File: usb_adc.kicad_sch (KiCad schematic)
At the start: 23 parts, among them IC1 PCM2903CDBR, SW1 SW_Push, SW2 SW_Push, SW3 SW_Push, U1 74LVC1G08, X1 ECS-120-8-36-CKM-TR3

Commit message: Resnap text to grid + add .gitignore
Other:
- company: (none) -> Tachyon PCBAs
- title: (none) -> USB ADC
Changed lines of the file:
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@@
 	(paper "A4")
 	(title_block
-		(date "2024-09-12")
+		(title "USB ADC")
+		(date "2024-09-15")
+		(rev "1")
+		(company "Tachyon PCBAs")
+		(comment 1 "first try surely")
+		(comment 2 "Built around the PCM2903C")
 	)
 	(junction
@@
 	(text "USB ADC"
 		(exclude_from_sim no)
-		(at 111.76 49.022 0)
+		(at 111.76 48.895 0)
 		(effects
 			(font
@@
 	(text "Pierce Oscillator (12MHz)"
 		(exclude_from_sim no)
-		(at 178.054 113.538 0)
+		(at 177.8 113.665 0)
 		(effects
 			(font
@@
 	(text "USB D+ Pull Up Logic"
 		(exclude_from_sim no)
-		(at 177.8 61.468 0)
+		(at 177.8 61.595 0)
 		(effects
 			(font
@@
 	(text "Suspension Indication LED"
 		(exclude_from_sim no)
-		(at 142.748 69.85 90)
+		(at 142.875 69.85 90)
 		(effects
 			(font
@@
 	(text "State machine control (Mute, Volume adj.)"
 		(exclude_from_sim no)
-		(at 178.054 17.018 0)
+		(at 177.8 17.145 0)
 		(effects
 			(font

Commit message: Started defining components
Man going down the capacitor dielectric rabbit hole eats up SO MUCH TIME
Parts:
- C1, C3, C4, C5: footprint Capacitor_SMD:C_0603_1608Metric_Pad1.08x0.95mm_HandSolder -> Capacitor_SMD:C_0805_2012Metric_Pad1.18x1.45mm_HandSolder; Mouser Part Number (none) -> 581-TAJA106K010TNJ
- C2: footprint (none) -> Capacitor_SMD:C_0805_2012Metric_Pad1.18x1.45mm_HandSolder; Mouser Part Number (none) -> 74-TMCP1E104KTRF
- C6, C7: Mouser Part Number (none) -> 581-06035A160FAT2A
- D1: value LED -> LTST-C193KRKT-2A; Mouser Part Number (none) -> 859-LTST-C193KRKT-2A
- R1, R10, R2, R4, R5, R6, R7, R8: footprint (none) -> Resistor_SMD:R_0603_1608Metric_Pad0.98x0.95mm_HandSolder
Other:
- moved on the sheet: D1
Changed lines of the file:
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@@
 	(wire
 		(pts
-			(xy 130.81 71.12) (xy 132.08 71.12)
+			(xy 133.35 71.12) (xy 132.08 71.12)
 		)
 		(stroke
@@
 	)
 	(label "~{SSPND}_R"
-		(at 130.81 71.12 180)
+		(at 133.35 71.12 0)
 		(fields_autoplaced yes)
 		(effects
@@
 				(size 1.27 1.27)
 			)
-			(justify right bottom)
+			(justify left bottom)
 		)
 	)
@@
 			)
 		)
-		(property "Footprint" "Capacitor_SMD:C_0603_1608Metric_Pad1.08x0.95mm_HandSolder"
+		(property "Footprint" "Capacitor_SMD:C_0805_2012Metric_Pad1.18x1.45mm_HandSolder"
 			(at 144.4752 119.38 0)
 			(effects
@@
 			)
 		)
-		(property "Datasheet" "~"
+		(property "Datasheet" "https://www.mouser.com/datasheet/2/40/TAJ_AUTO-3165268.pdf"
 			(at 143.51 115.57 0)
 			(effects
@@
 			)
 		)
+		(property "Mouser Part Number" "581-TAJA106K010TNJ"
+			(at 143.51 115.57 0)
+			(effects
+				(font
+					(size 1.27 1.27)
+				)
+				(hide yes)
+			)
+		)
 		(pin "1"
 		)
@@
 			)
 		)
-		(property "Footprint" "Capacitor_SMD:C_0603_1608Metric_Pad1.08x0.95mm_HandSolder"
+		(property "Footprint" "Capacitor_SMD:C_0805_2012Metric_Pad1.18x1.45mm_HandSolder"
 			(at 150.8252 93.98 0)
 			(effects
@@
 			)
 		)
-		(property "Datasheet" "~"
+		(property "Datasheet" "https://www.mouser.com/datasheet/2/40/TAJ_AUTO-3165268.pdf"
 			(at 149.86 90.17 0)
 			(effects
@@
 			)
 		)
+		(property "Mouser Part Number" "581-TAJA106K010TNJ"
+			(at 149.86 90.17 0)
+			(effects
+				(font
+					(size 1.27 1.27)
+				)
+				(hide yes)
+			)
+		)
 		(pin "1"
 		)
@@
 			)
 		)
-		(property "Footprint" ""
+		(property "Footprint" "Resistor_SMD:R_0603_1608Metric_Pad0.98x0.95mm_HandSolder"
 			(at 207.772 33.02 90)
 			(effects
@@
 			)
 		)
-		(property "Datasheet" "~"
+		(property "Datasheet" "https://www.mouser.com/datasheet/2/40/C0GNP0_Dielectric-2952720.pdf"
 			(at 223.52 147.32 0)
 			(effects
@@
 			)
 		)
+		(property "Mouser Part Number" "581-06035A160FAT2A"
+			(at 223.52 147.32 0)
+			(effects
+				(font
+					(size 1.27 1.27)
+				)
+				(hide yes)
+			)
+		)
 		(pin "1"
 		)
@@
 			)
 		)
-		(property "Footprint" ""
+		(property "Footprint" "Resistor_SMD:R_0603_1608Metric_Pad0.98x0.95mm_HandSolder"
 			(at 236.22 85.598 90)
 			(effects
@@
 			)
 		)
-		(property "Footprint" ""
+		(property "Footprint" "Capacitor_SMD:C_0805_2012Metric_Pad1.18x1.45mm_HandSolder"
 			(at 180.6448 73.66 0)
 			(effects
@@
 			)
 		)
-		(property "Datasheet" "~"
+		(property "Datasheet" "https://www.vishay.com/docs/40179/tmcp.pdf"
 			(at 181.61 77.47 0)
 			(effects
@@
 			)
 		)
+		(property "Mouser Part Number" "74-TMCP1E104KTRF"
+			(at 181.61 77.47 0)
+			(effects
+				(font
+					(size 1.27 1.27)
+				)
+				(hide yes)
+			)
+		)
 		(pin "2"
 		)
@@
 			)
 		)
-		(property "Footprint" ""
+		(property "Footprint" "Resistor_SMD:R_0603_1608Metric_Pad0.98x0.95mm_HandSolder"
 			(at 191.262 91.44 90)
 			(effects
@@
 	(symbol
 		(lib_id "Device:LED")
-		(at 132.08 66.04 90)
+		(at 132.08 66.04 270)
+		(mirror x)
 		(unit 1)
 		(exclude_from_sim no)
@@
 		(fields_autoplaced yes)
 		(property "Reference" "D1"
-			(at 135.89 66.3574 90)
+			(at 128.27 66.3574 90)
 			(effects
 				(font
@@
 			)
 		)
-		(property "Value" "LED"
-			(at 135.89 68.8974 90)
+		(property "Value" "LTST-C193KRKT-2A"
+			(at 128.27 68.8974 90)
 			(effects
 				(font
@@
 			)
 		)
-		(property "Datasheet" "~"
+		(property "Datasheet" "https://www.mouser.com/datasheet/2/239/lite-on_lite-s-a0004283979-1-1749859.pdf"
 			(at 132.08 66.04 0)
 			(effects
@@
 			)
 		)
+		(property "Mouser Part Number" "859-LTST-C193KRKT-2A"
+			(at 132.08 66.04 0)
+			(effects
+				(font
+					(size 1.27 1.27)
+				)
+				(hide yes)
+			)
+		)
 		(pin "2"
 		)
@@
 			)
 		)
-		(property "Footprint" ""
+		(property "Footprint" "Resistor_SMD:R_0603_1608Metric_Pad0.98x0.95mm_HandSolder"
 			(at 81.28 84.328 90)
 			(effects
@@
 			)
 		)
-		(property "Footprint" ""
+		(property "Footprint" "Resistor_SMD:R_0603_1608Metric_Pad0.98x0.95mm_HandSolder"
 			(at 182.372 33.02 90)
 			(effects
@@
 			)
 		)
-		(property "Footprint" "Capacitor_SMD:C_0603_1608Metric_Pad1.08x0.95mm_HandSolder"
+		(property "Footprint" "Capacitor_SMD:C_0805_2012Metric_Pad1.18x1.45mm_HandSolder"
 			(at 87.63 116.5352 0)
 			(effects
@@
 			)
 		)
-		(property "Datasheet" "~"
+		(property "Datasheet" "https://www.mouser.com/datasheet/2/40/TAJ_AUTO-3165268.pdf"
 			(at 83.82 115.57 0)
 			(effects
@@
 			)
 		)
+		(property "Mouser Part Number" "581-TAJA106K010TNJ"
+			(at 83.82 115.57 0)
+			(effects
+				(font
+					(size 1.27 1.27)
+				)
+				(hide yes)
+			)
+		)
 		(pin "1"
 		)
@@
 			)
 		)
-		(property "Footprint" ""
+		(property "Footprint" "Resistor_SMD:R_0603_1608Metric_Pad0.98x0.95mm_HandSolder"
 			(at 231.902 33.02 90)
 			(effects
@@
 		(lib_id "power:VDD")
 		(at 132.08 60.96 0)
+		(mirror y)
 		(unit 1)
 		(exclude_from_sim no)
@@
 			)
 		)
-		(property "Footprint" "Capacitor_SMD:C_0603_1608Metric_Pad1.08x0.95mm_HandSolder"
+		(property "Footprint" "Capacitor_SMD:C_0805_2012Metric_Pad1.18x1.45mm_HandSolder"
 			(at 64.4652 114.3 0)
 			(effects
@@
 			)
 		)
-		(property "Datasheet" "~"
+		(property "Datasheet" "https://www.mouser.com/datasheet/2/40/TAJ_AUTO-3165268.pdf"
 			(at 63.5 110.49 0)
 			(effects
@@
 			)
 		)
+		(property "Mouser Part Number" "581-TAJA106K010TNJ"
+			(at 63.5 110.49 0)
+			(effects
+				(font
+					(size 1.27 1.27)
+				)
+				(hide yes)
+			)
+		)
 		(pin "1"
 		)
@@
 			)
 		)
-		(property "Footprint" ""
+		(property "Footprint" "Resistor_SMD:R_0603_1608Metric_Pad0.98x0.95mm_HandSolder"
 			(at 81.28 86.868 90)
 			(effects
@@
 			)
 		)
-		(property "Datasheet" "~"
+		(property "Datasheet" "https://www.mouser.com/datasheet/2/40/C0GNP0_Dielectric-2952720.pdf"
 			(at 200.66 147.32 0)
 			(effects
@@
 			)
 		)
+		(property "Mouser Part Number" "581-06035A160FAT2A"
+			(at 200.66 147.32 0)
+			(effects
+				(font
+					(size 1.27 1.27)
+				)
+				(hide yes)
+			)
+		)
 		(pin "1"
 		)
@@
 			)
 		)
-		(property "Footprint" ""
+		(property "Footprint" "Resistor_SMD:R_0603_1608Metric_Pad0.98x0.95mm_HandSolder"
 			(at 130.302 76.2 90)
 			(effects

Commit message: Fully define components
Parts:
- R1, R2, R4, R8: Mouser Part Number (none) -> 667-ERA-3AEB152V
- R10, R13: Mouser Part Number (none) -> 652-CR0603FX-1004ELF
- R5: Mouser Part Number (none) -> 71-CRCW08055K60FKEAC
- R6, R7: Mouser Part Number (none) -> 652-CR0603FX-22R0ELF
- U1: Mouser Part Number (none) -> 771-74LVC1G08GV
- X1: Mouser Part Number (none) -> 520-120-8-36-CKM-TR3
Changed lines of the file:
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@@
+			)
+		)
+		(property "Mouser Part Number" "771-74LVC1G08GV"
+			(at 209.55 83.82 0)
+			(effects
+				(font
+					(size 1.27 1.27)
+				)
+				(hide yes)
 			)
 		)
@@
 			)
 		)
-		(property "Datasheet" "~"
+		(property "Datasheet" "https://www.mouser.com/datasheet/2/315/AOA0000C307-1149632.pdf"
 			(at 209.55 33.02 0)
 			(effects
@@
 			)
 		)
+		(property "Mouser Part Number" "667-ERA-3AEB152V"
+			(at 209.55 33.02 0)
+			(effects
+				(font
+					(size 1.27 1.27)
+				)
+				(hide yes)
+			)
+		)
 		(pin "2"
 		)
@@
 			)
 		)
-		(property "Datasheet" "~"
+		(property "Datasheet" "https://www.mouser.com/datasheet/2/54/cr-1858361.pdf"
 			(at 212.09 124.46 0)
 			(effects
@@
 			)
 		)
+		(property "Mouser Part Number" "652-CR0603FX-1004ELF"
+			(at 212.09 124.46 0)
+			(effects
+				(font
+					(size 1.27 1.27)
+				)
+				(hide yes)
+			)
+		)
 		(pin "1"
 		)
@@
 			)
 		)
-		(property "Datasheet" "~"
+		(property "Datasheet" "https://www.mouser.com/datasheet/2/315/AOA0000C307-1149632.pdf"
 			(at 236.22 83.82 0)
 			(effects
@@
 			)
 		)
+		(property "Mouser Part Number" "667-ERA-3AEB152V"
+			(at 236.22 83.82 0)
+			(effects
+				(font
+					(size 1.27 1.27)
+				)
+				(hide yes)
+			)
+		)
 		(pin "2"
 		)
@@
 			)
 		)
-		(property "Datasheet" "~"
+		(property "Datasheet" "https://www.mouser.com/datasheet/2/54/cr-1858361.pdf"
 			(at 193.04 91.44 0)
 			(effects
@@
 		)
 		(property "Description" "Resistor"
+			(at 193.04 91.44 0)
+			(effects
+				(font
+					(size 1.27 1.27)
+				)
+				(hide yes)
+			)
+		)
+		(property "Mouser Part Number" "652-CR0603FX-1004ELF"
 			(at 193.04 91.44 0)
 			(effects
@@
 			)
 		)
-		(property "Datasheet" "~"
+		(property "Datasheet" "https://www.mouser.com/datasheet/2/54/cr-1858361.pdf"
 			(at 81.28 82.55 0)
 			(effects
@@
 			)
 		)
+		(property "Mouser Part Number" "652-CR0603FX-22R0ELF"
+			(at 81.28 82.55 0)
+			(effects
+				(font
+					(size 1.27 1.27)
+				)
+				(hide yes)
+			)
+		)
 		(pin "2"
 		)
@@
 			)
 		)
-		(property "Datasheet" "~"
+		(property "Datasheet" "https://www.mouser.com/datasheet/2/315/AOA0000C307-1149632.pdf"
 			(at 184.15 33.02 0)
 			(effects
@@
 		)
 		(property "Description" "Resistor"
+			(at 184.15 33.02 0)
+			(effects
+				(font
+					(size 1.27 1.27)
+				)
+				(hide yes)
+			)
+		)
+		(property "Mouser Part Number" "667-ERA-3AEB152V"
 			(at 184.15 33.02 0)
 			(effects
@@
 			)
 		)
+		(property "Mouser Part Number" "520-120-8-36-CKM-TR3"
+			(at 212.09 142.24 0)
+			(effects
+				(font
+					(size 1.27 1.27)
+				)
+				(hide yes)
+			)
+		)
 		(pin "2"
 		)
@@
 			)
 		)
-		(property "Datasheet" "~"
+		(property "Datasheet" "https://www.mouser.com/datasheet/2/315/AOA0000C307-1149632.pdf"
 			(at 233.68 33.02 0)
 			(effects
@@
 		)
 		(property "Description" "Resistor"
+			(at 233.68 33.02 0)
+			(effects
+				(font
+					(size 1.27 1.27)
+				)
+				(hide yes)
+			)
+		)
+		(property "Mouser Part Number" "667-ERA-3AEB152V"
 			(at 233.68 33.02 0)
 			(effects
@@
 			)
 		)
-		(property "Datasheet" "~"
+		(property "Datasheet" "https://www.mouser.com/datasheet/2/54/cr-1858361.pdf"
 			(at 81.28 85.09 0)
 			(effects
@@
 		)
 		(property "Description" "Resistor"
+			(at 81.28 85.09 0)
+			(effects
+				(font
+					(size 1.27 1.27)
+				)
+				(hide yes)
+			)
+		)
+		(property "Mouser Part Number" "652-CR0603FX-22R0ELF"
 			(at 81.28 85.09 0)
 			(effects
@@
 			)
 		)
-		(property "Datasheet" "~"
+		(property "Datasheet" "https://www.vishay.com/doc?28773"
 			(at 132.08 76.2 0)
 			(effects
@@
 			(at 132.08 76.2 0)
 			(effects
+				(font
+					(size 1.27 1.27)
+				)
+				(hide yes)
+			)
+		)
+		(property "Mouser Part Number" "71-CRCW08055K60FKEAC"
+			(at 132.08 76.2 0)
+			(effects

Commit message: Replace S/PIDF RCA jack with a singular one since I won't need an input one
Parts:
- SW1, SW2, SW3: value SW_Push -> MX1A-11NW; footprint (none) -> binauralmic:SW_MX; Mouser Part Number (none) -> 540-MX1A-11NW
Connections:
- net DIN: no longer names the net of IC1.24 (DIN)
- no-connect marks 2 -> 3
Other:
- moved on the sheet: R1, R2, R4, SW1, SW2, SW3

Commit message: Removing extraneous peripherals
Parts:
- removed R1, R2, R4: 1.5k, Resistor_SMD:R_0603_1608Metric_Pad0.98x0.95mm_HandSolder, symbol Device:R
- removed SW1, SW2, SW3: MX1A-11NW, binauralmic:SW_MX, symbol Switch:SW_Push
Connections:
- net HID0: no longer names the net of IC1.5 (HID0)
- net HID1: no longer names the net of IC1.6 (HID1)
- net HID2: no longer names the net of IC1.7 (HID2)
- no-connect marks 3 -> 6
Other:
- note removed: "State machine control (Mute, Volume adj.)"
- moved on the sheet: C2, C6, C7, R10, R13, R8, U1, X1

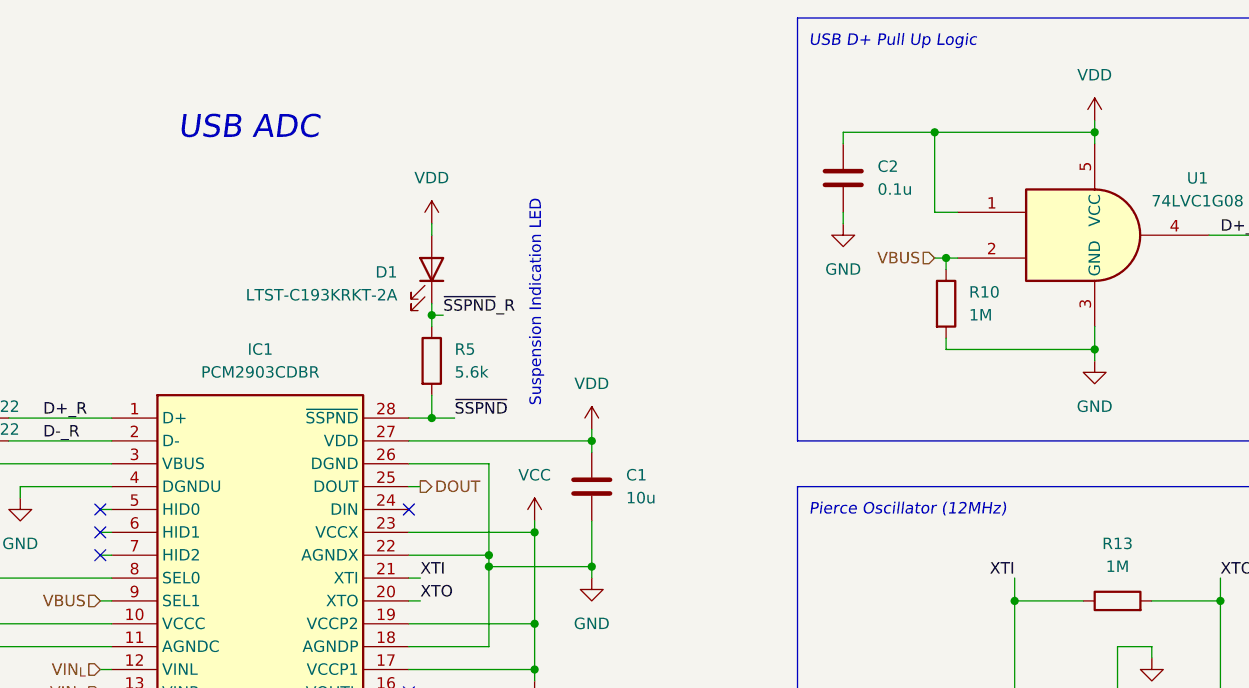
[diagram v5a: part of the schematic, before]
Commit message: Remove potentiometer
Will have to find a different solution for volume control
Just do it OS-side?
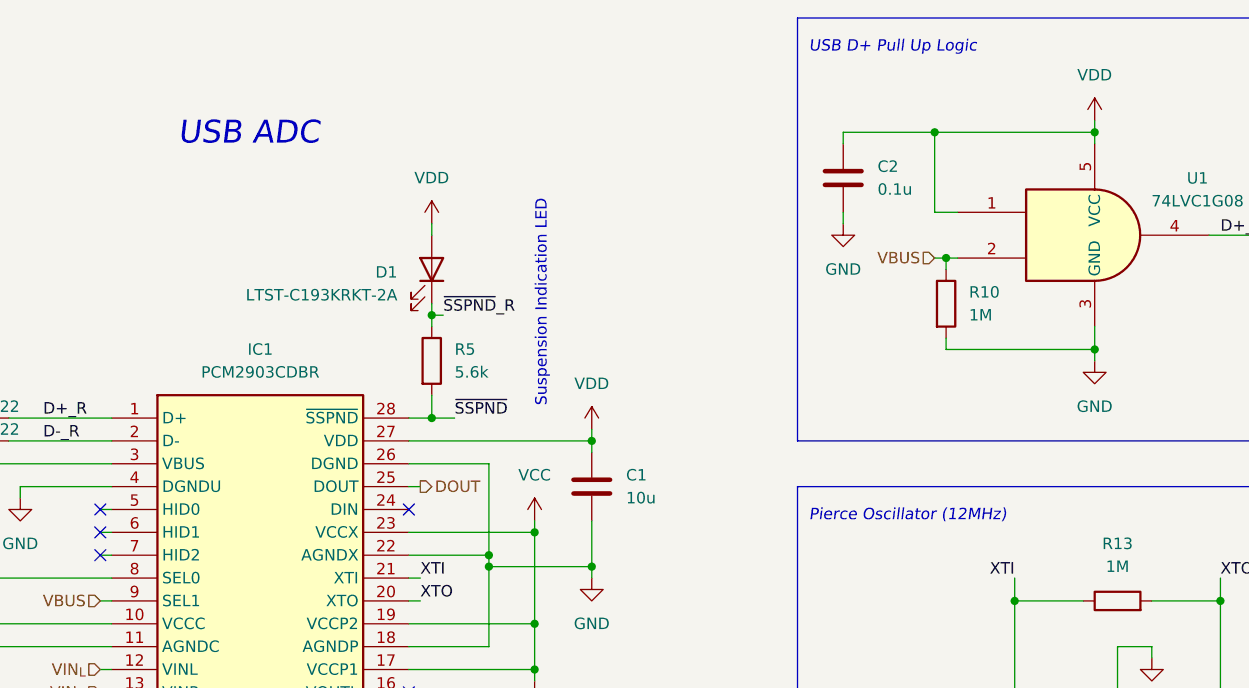
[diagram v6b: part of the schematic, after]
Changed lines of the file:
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@@
 	(text "USB ADC"
 		(exclude_from_sim no)
-		(at 111.76 48.895 0)
+		(at 111.76 49.53 0)
 		(effects
 			(font
@@
 	(text "Pierce Oscillator (12MHz)"
 		(exclude_from_sim no)
-		(at 173.99 92.075 0)
+		(at 173.99 92.71 0)
 		(effects
 			(font
@@
 	(text "USB D+ Pull Up Logic"
 		(exclude_from_sim no)
-		(at 173.99 40.005 0)
+		(at 173.99 40.64 0)
 		(effects
 			(font
@@
 	(text "Suspension Indication LED"
 		(exclude_from_sim no)
-		(at 142.875 69.85 90)
+		(at 143.51 69.85 90)
 		(effects
 			(font
